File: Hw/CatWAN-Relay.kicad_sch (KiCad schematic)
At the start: 53 parts, among them J10 USB_B, J2 INPUTS, J3 OUTPUTS, J4 SWD, J5 Serial, Q1 MMBT2222A, Q2 MMBT2222A, Q3 MMBT2222A, U2 RFM95W-915-868, U3 LTV-817, U4 LTV-817, U5 LTV-817, U6 LM2596_DC-DC, U7 AP2114H-3.3TRG1, U8 ESP32-C6-WROOM-1U-N4, Y1 UD2-3NU, Y2 UD2-3NU, Y3 UD2-3NU

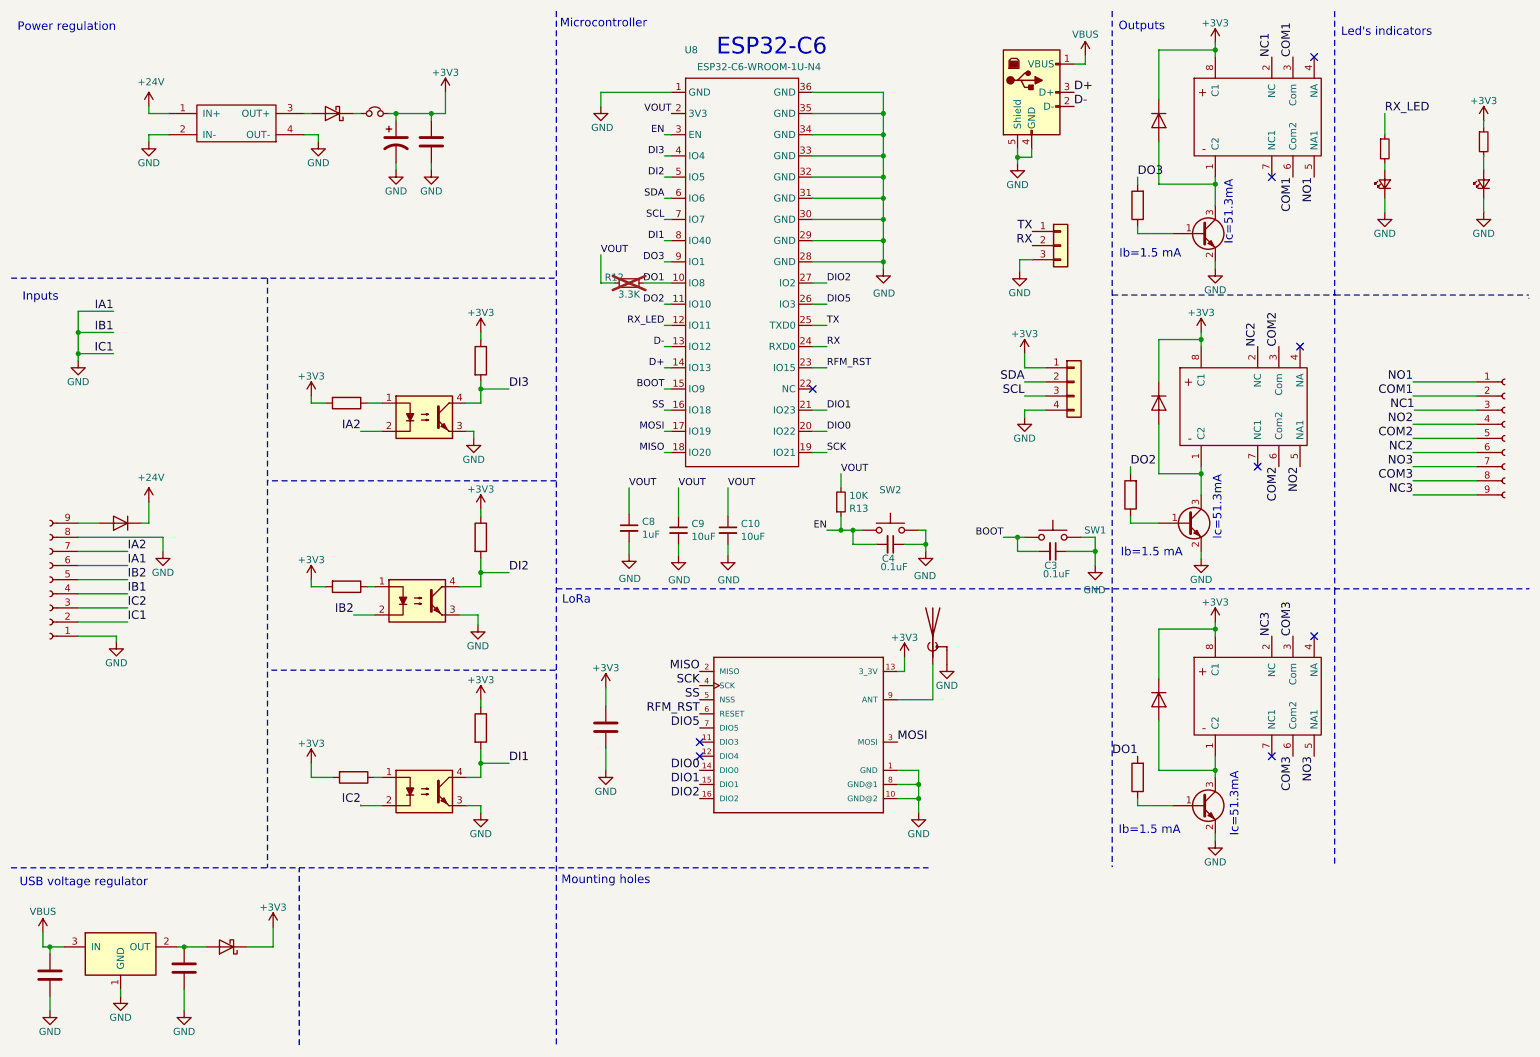
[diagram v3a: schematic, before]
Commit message: feat(hw): USB C schematic changed & fusible added & references added
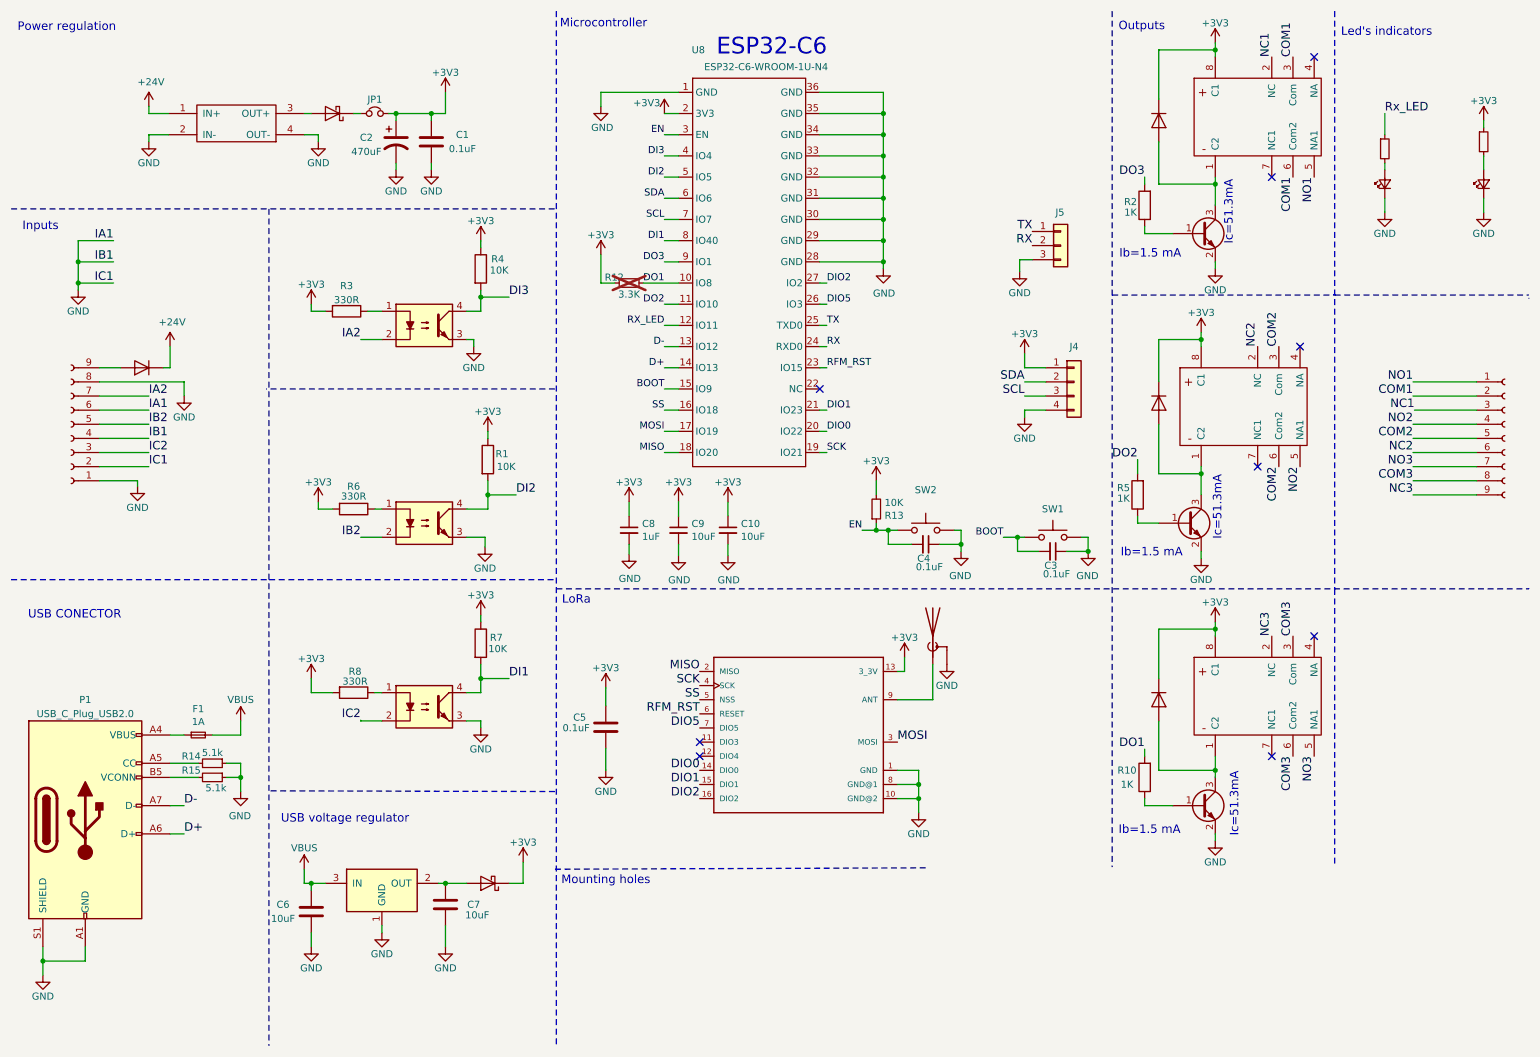
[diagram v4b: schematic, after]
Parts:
- removed J10: USB_B, agroin:C393939, symbol CatWAN-Relay-rescue:USB_B-agroin-rescue
- added F1: 1A, Fuse:Fuse_0603_1608Metric, symbol Device:Fuse_Small
- added P1: USB_C_Plug_USB2.0, agroin:C393939, symbol Connector:USB_C_Plug_USB2.0
- added R14, R15: 5.1k, Resistor_SMD:R_0603_1608Metric, symbol Device:R_Small
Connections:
- net VOUT is gone; now on net +3V3: C10.1, C8.1, C9.1, R12.2, R13.2, U8.2 (3V3)
- net D+: now also P1.A6 (D+)
- net D-: now also P1.A7 (D-)
- net GND: now also P1.A1 (GND), P1.A12 (GND), P1.B1 (GND), P1.B12 (GND), P1.S1 (SHIELD), R14.1, R15.1
- net RX_LED: no longer R11.1
- net VBUS: now also F1.2
- new net: F1.1, P1.A4 (VBUS), P1.A9 (VBUS), P1.B4 (VBUS), P1.B9 (VBUS)
- new net: P1.A5 (CC), R14.2
- new net: P1.B5 (VCONN), R15.2
- new net Rx_LED: R11.1
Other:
- note added: "USB CONECTOR"
- moved on the sheet: C4, R13, SW2, U8

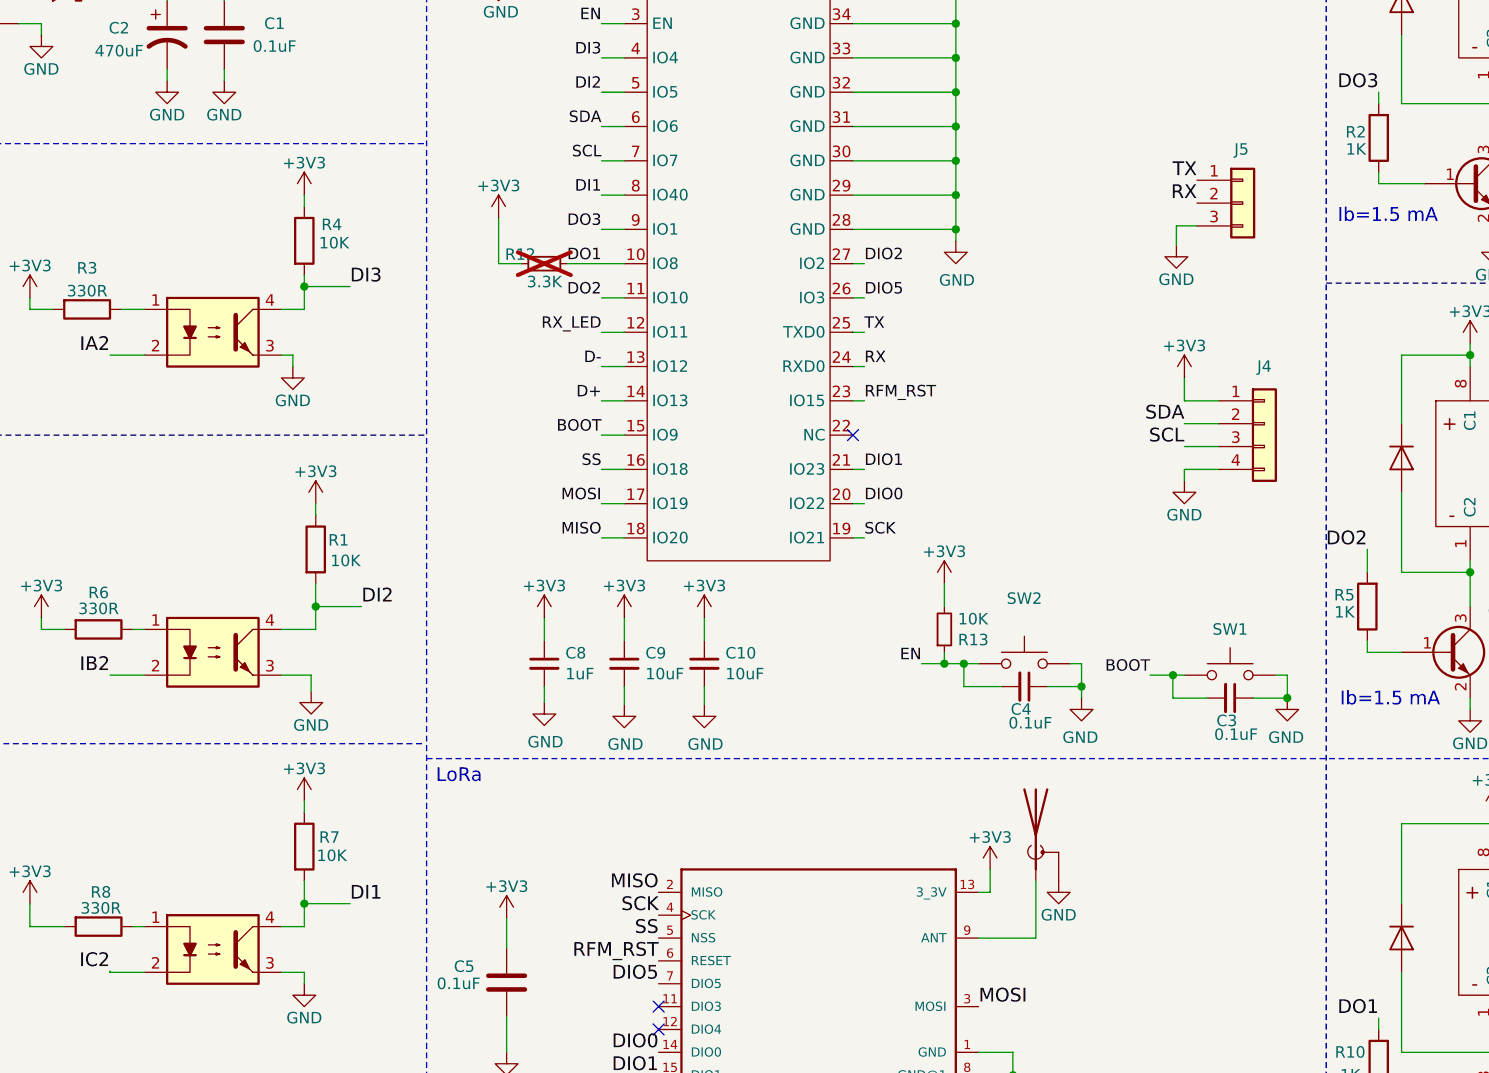
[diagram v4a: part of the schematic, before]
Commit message: feat: UPDATE BOM & diode changed
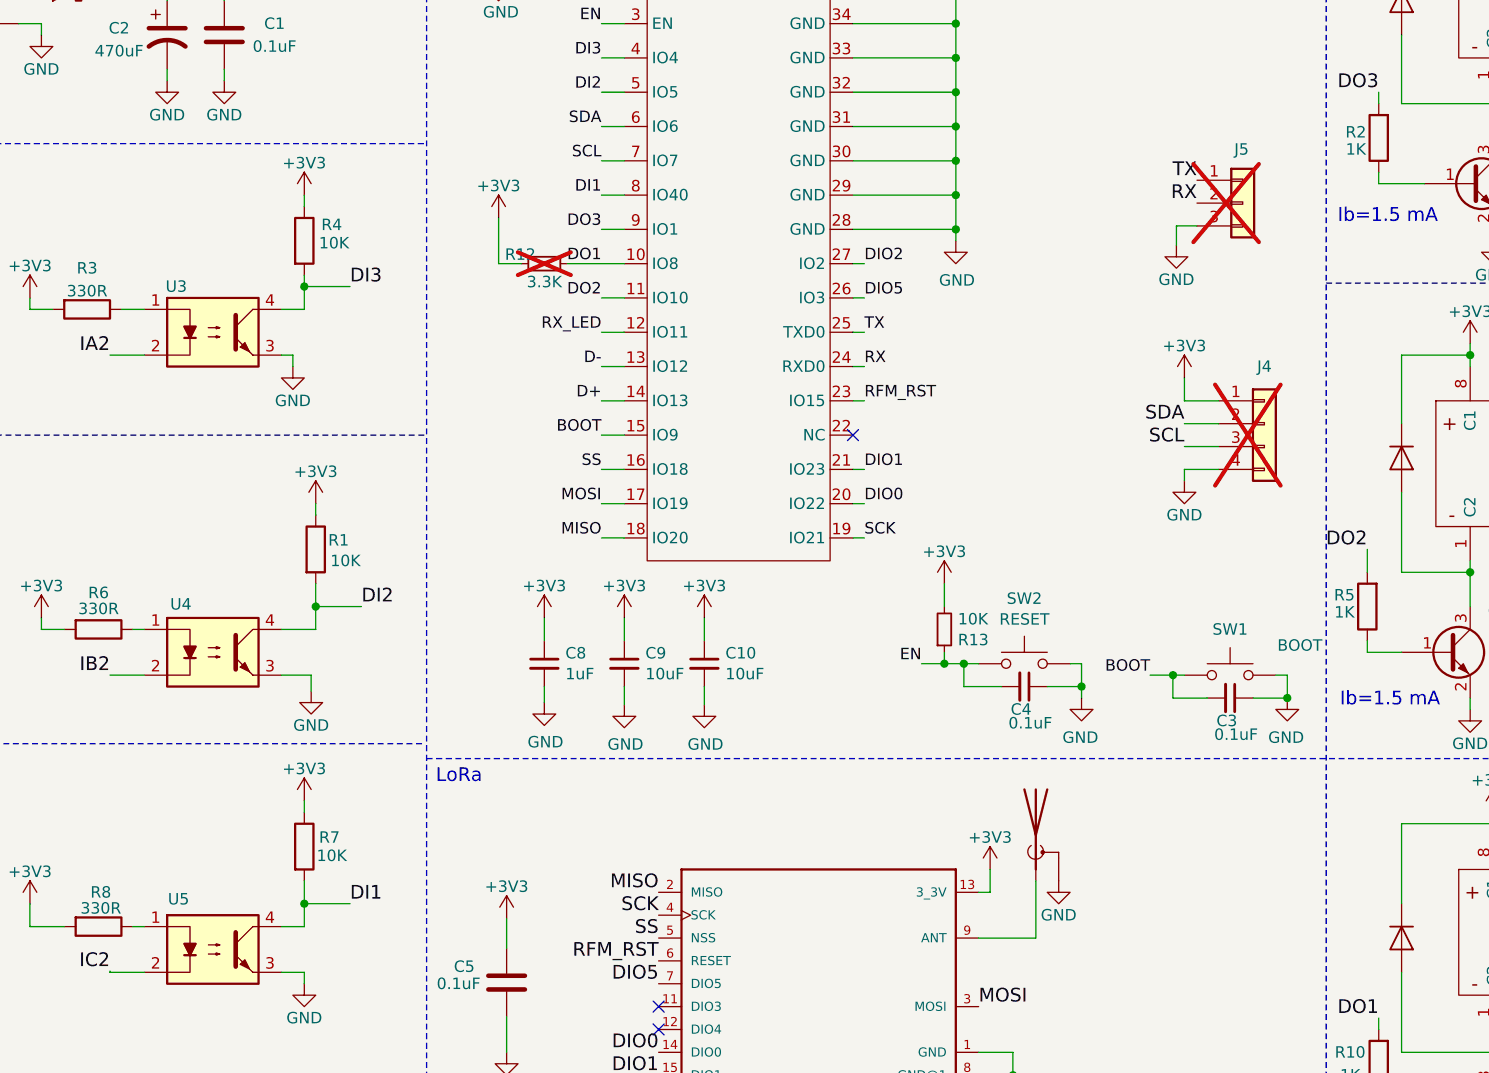
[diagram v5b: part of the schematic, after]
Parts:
- AE1: LCSC# 2337019-1 -> C7426714; Proveedor (none) -> LCSC
- C1, C5: LCSC# (none) -> C15725; Proveedor (none) -> LCSC; manf# 885012207072 -> (none)
- C10, C9: Proveedor JLCPCB -> LCSC; manf# GRM188R61E106KA73J -> (none)
- C2: LCSC# (none) -> C5354997; Proveedor (none) -> LCSC; manf# UUR0G471MCL1GS -> (none)
- C3, C4: LCSC# C478888 -> C15725; Proveedor JLCPCB -> LCSC; manf# KAM15AR71C104KM -> (none)
- C6, C7: LCSC# (none) -> C85713; Proveedor (none) -> LCSC; manf# GRM21BC80J106KE19L -> (none)
- C8: Proveedor JLCPCB -> LCSC; manf# TMK107BJ105KA8T -> (none)
- D1, D2, D3: value FM4007W-W -> RS1M; footprint agroin:F4007 -> Diode_SMD:D_SMA; LCSC# (none) -> C513461; Proveedor (none) -> LCSC; manf# FM4007W-W -> (none)
- D4: value FM4007W-W -> RS1M; footprint Diode_SMD:D_SOD-123 -> Diode_SMD:D_SMA; LCSC# (none) -> C513461; Proveedor (none) -> LCSC; manf# FM4007W-W -> (none)
- D5, D8: LCSC# (none) -> C130880; Proveedor (none) -> LCSC; manf# MBR120VLSFT3G -> (none)
- D6: LCSC# (none) -> C130114; Proveedor (none) -> LCSC
- D7: LCSC# (none) -> C205442; Proveedor (none) -> LCSC
- F1: LCSC# C182438 -> C151139; Proveedor (none) -> LCSC
- J2, J3: Proveedor (none) -> STEREN
- J4: value SWD -> I2C; now not fitted
- J5: now not fitted
- JP1: Proveedor (none) -> STEREN; manf# (none) -> PINES
- P1: LCSC# (none) -> C393939; Proveedor (none) -> LCSC
- Q1, Q2, Q3: LCSC# (none) -> C916372; Proveedor (none) -> LCSC
- R1, R4, R7: LCSC# (none) -> C15401; Proveedor (none) -> LCSC; manf# RC0402FR-1010KL -> (none)
- R10, R2, R5: LCSC# (none) -> C115325; Proveedor (none) -> LCSC; manf# RC0805FR-071KL -> (none)
- R11, R9: LCSC# (none) -> C22787; Proveedor (none) -> LCSC
- R12: LCSC# C403480 -> (none); Proveedor JLCPCB -> (none); manf# ERJ-3GEYJ332V -> (none)
- R13: LCSC# C217281 -> C15401; Proveedor JLCPCB -> LCSC; manf# RMC1/16K1002DTP -> (none)
- R14, R15: LCSC# C407575 -> C122969; Proveedor (none) -> LCSC
- R3, R6, R8: LCSC# (none) -> C25231; Proveedor (none) -> LCSC; manf# CRCW08052K20FKEB -> (none)
- SW1: value ~ -> BOOT
- SW2: value ~ -> RESET
- U2: Proveedor (none) -> MOUSER
- U3, U4, U5: LCSC# (none) -> C479627; Proveedor (none) -> LCSC
- U6: Proveedor (none) -> UNIT
- U7: LCSC# (none) -> C150716; Proveedor (none) -> LCSC
- Y1, Y2, Y3: LCSC# (none) -> C90259; Proveedor (none) -> LCSC

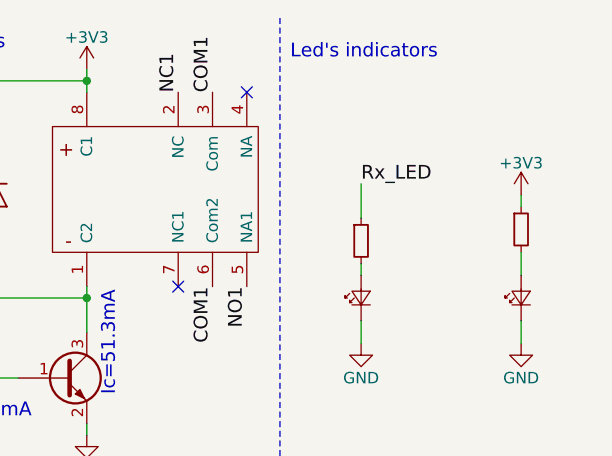
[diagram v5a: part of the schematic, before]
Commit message: fix: label RX led
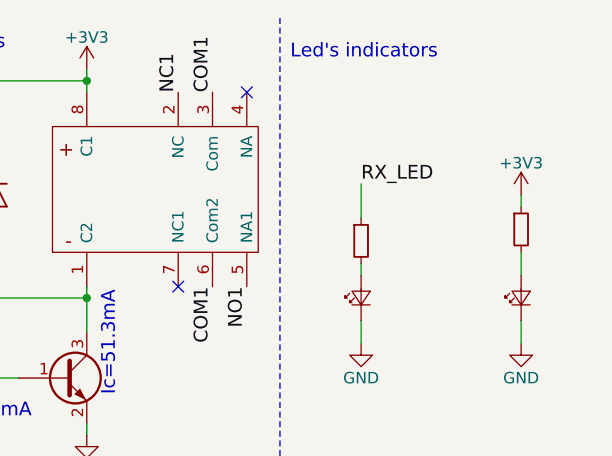
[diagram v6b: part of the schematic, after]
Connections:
- net Rx_LED is gone; now on net RX_LED: R11.1
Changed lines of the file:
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@@
 		)
 	)
-	(label "Rx_LED"
+	(label "RX_LED"
 		(at 259.08 30.48 0)
 		(fields_autoplaced yes)

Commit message: feat(hw): Footprint added
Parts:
- U8: footprint agroin:XCVR_ESP32-C6-WROOM-1-N8 -> PCM_Espressif:ESP32-C6-WROOM-1U
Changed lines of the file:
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@@
 			)
 		)
-		(property "Footprint" "agroin:XCVR_ESP32-C6-WROOM-1-N8"
+		(property "Footprint" "PCM_Espressif:ESP32-C6-WROOM-1U"
 			(at 146.812 11.684 0)
 			(effects
